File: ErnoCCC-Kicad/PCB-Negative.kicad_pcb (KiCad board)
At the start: 2 copper layers, 197 x 137 mm, 0 parts

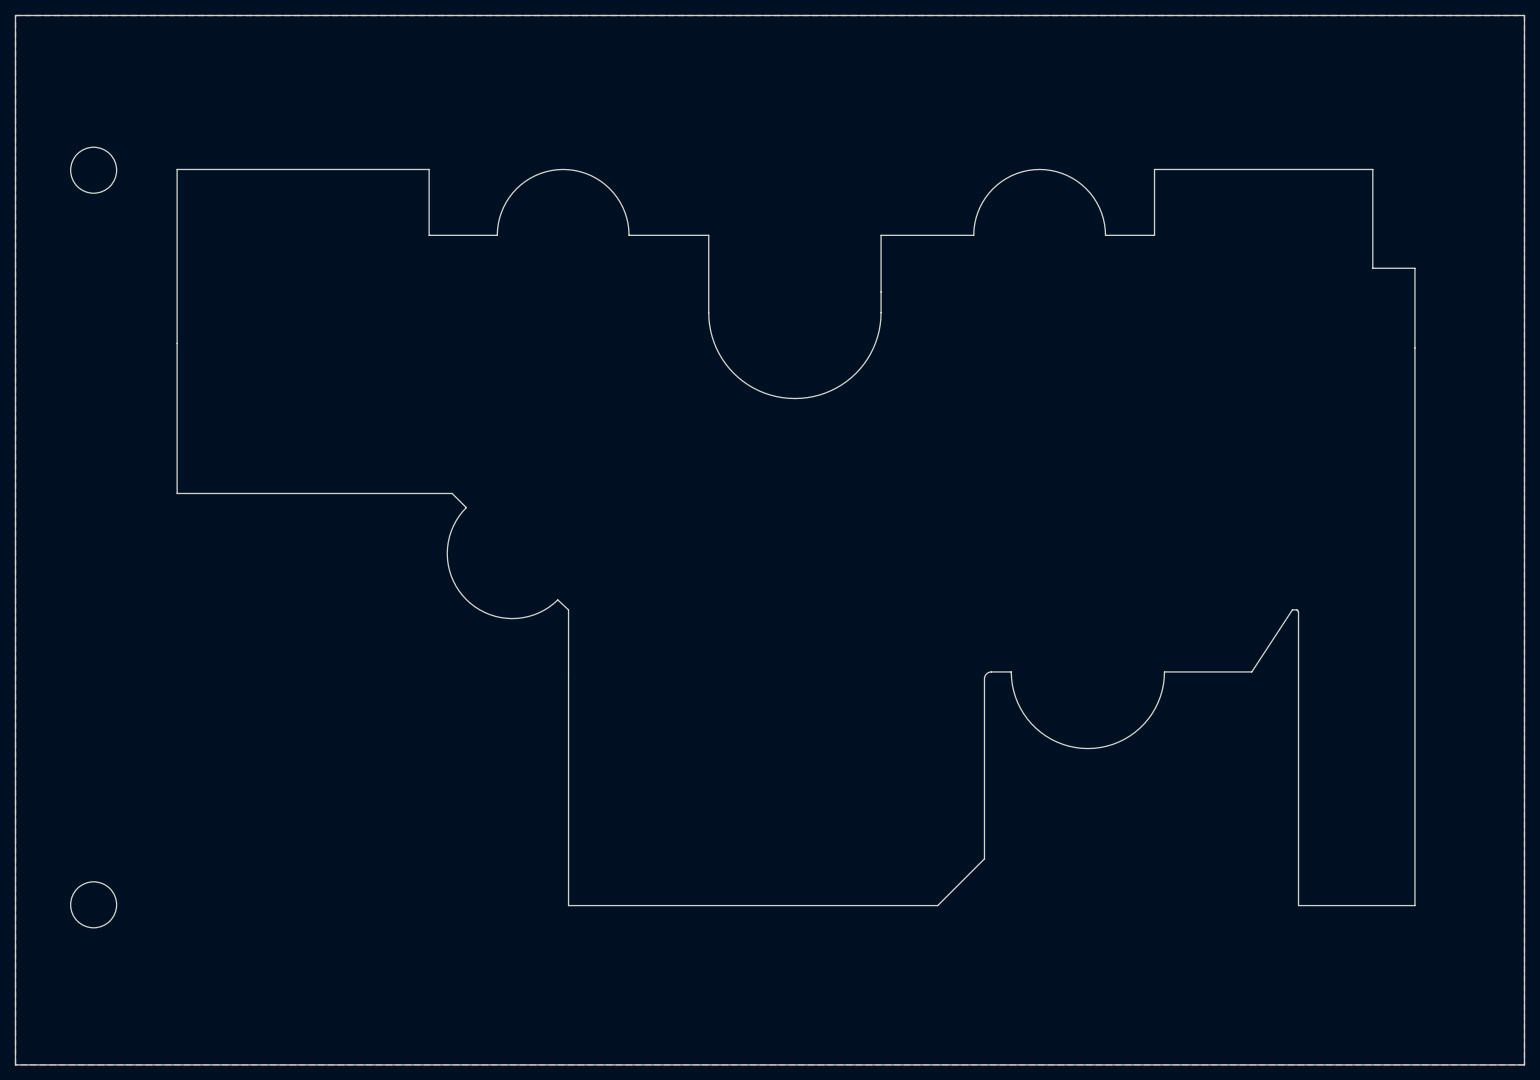
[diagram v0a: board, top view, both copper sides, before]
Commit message: Rounding Corners, making fidicules actually match
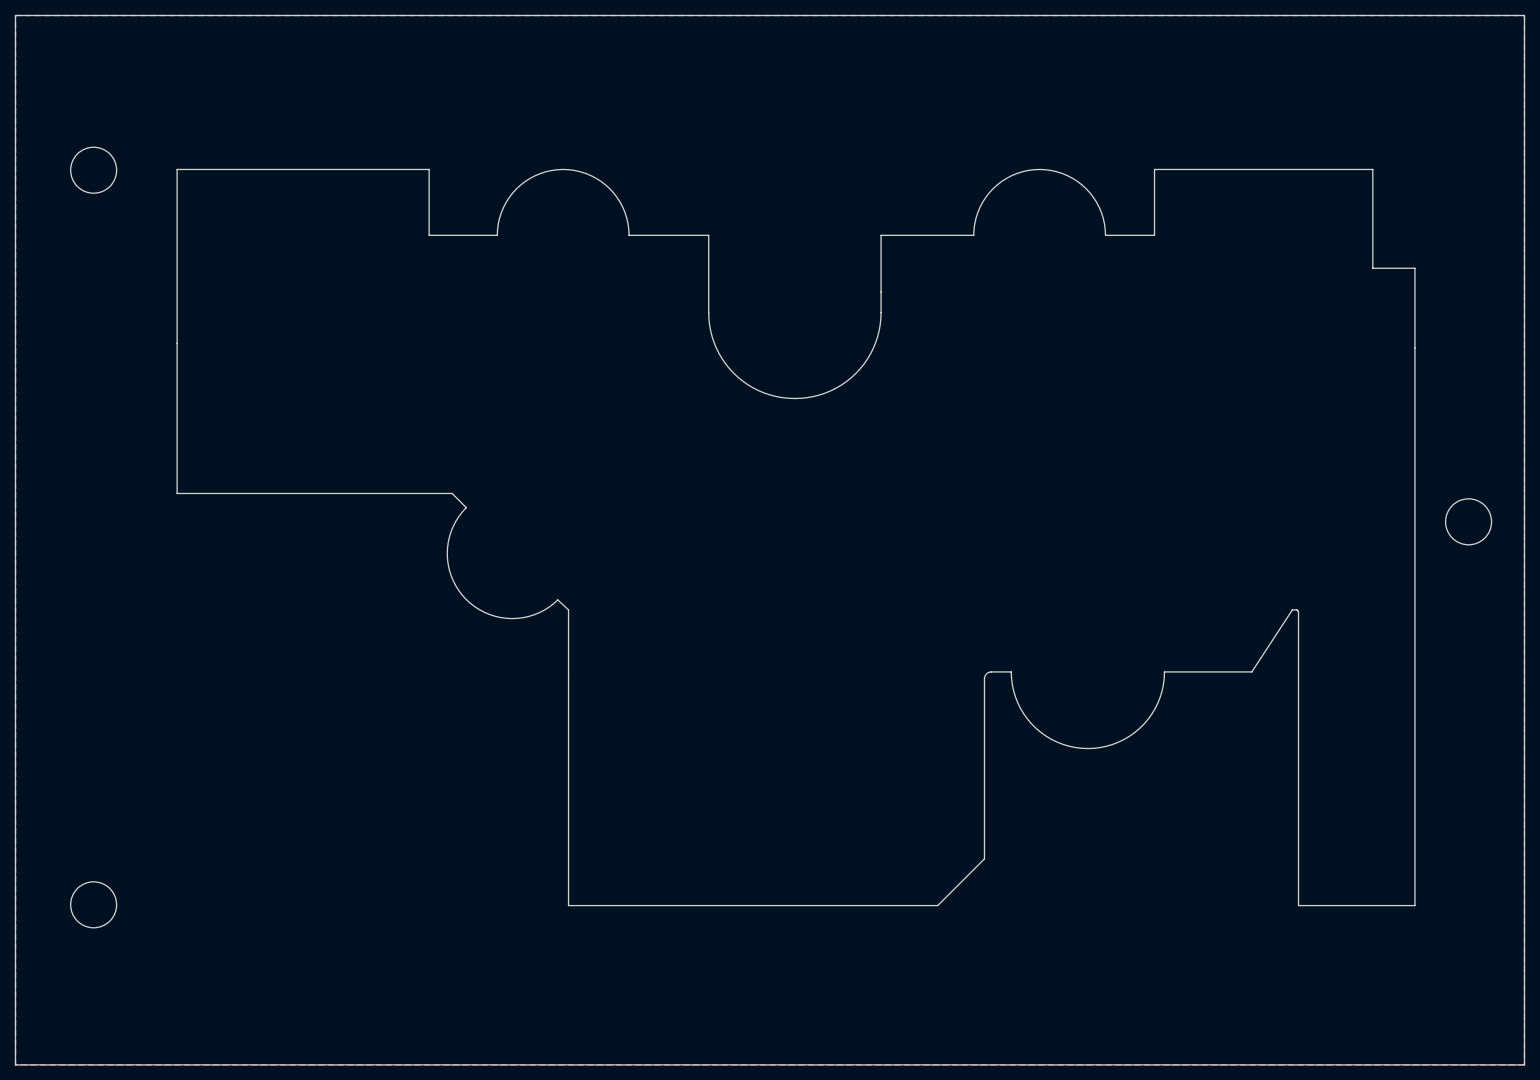
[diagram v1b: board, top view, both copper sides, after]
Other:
- outline, holes or cut-outs redrawn
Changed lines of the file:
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@@
   (general
     (thickness 1.6)
-    (drawings 49)
+    (drawings 50)
     (tracks 0)
     (zones 0)
@@
     (uvia_drill 0.1)
   )
-  (gr_circle (center 58.2 138.1) (end 61.2 138.1) (layer Edge.Cuts) (width 0.05))
-  (gr_circle (center 58.2 42.2) (end 61.2 42.2) (layer Edge.Cuts) (width 0.05))
+  (gr_circle (center 237.7 88.1) (end 240.7 88.1) (layer Edge.Cuts) (width 0.01))
+  (gr_circle (center 58.2 138.1) (end 61.2 138.1) (layer Edge.Cuts) (width 0.01))
+  (gr_circle (center 58.2 42.2) (end 61.2 42.2) (layer Edge.Cuts) (width 0.01))
   (gr_line (start 48 22) (end 69 22) (layer Edge.Cuts) (width 0.05))
   (gr_line (start 48 159) (end 48 22) (layer Edge.Cuts) (width 0.05))
